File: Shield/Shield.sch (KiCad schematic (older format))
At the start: 0 parts

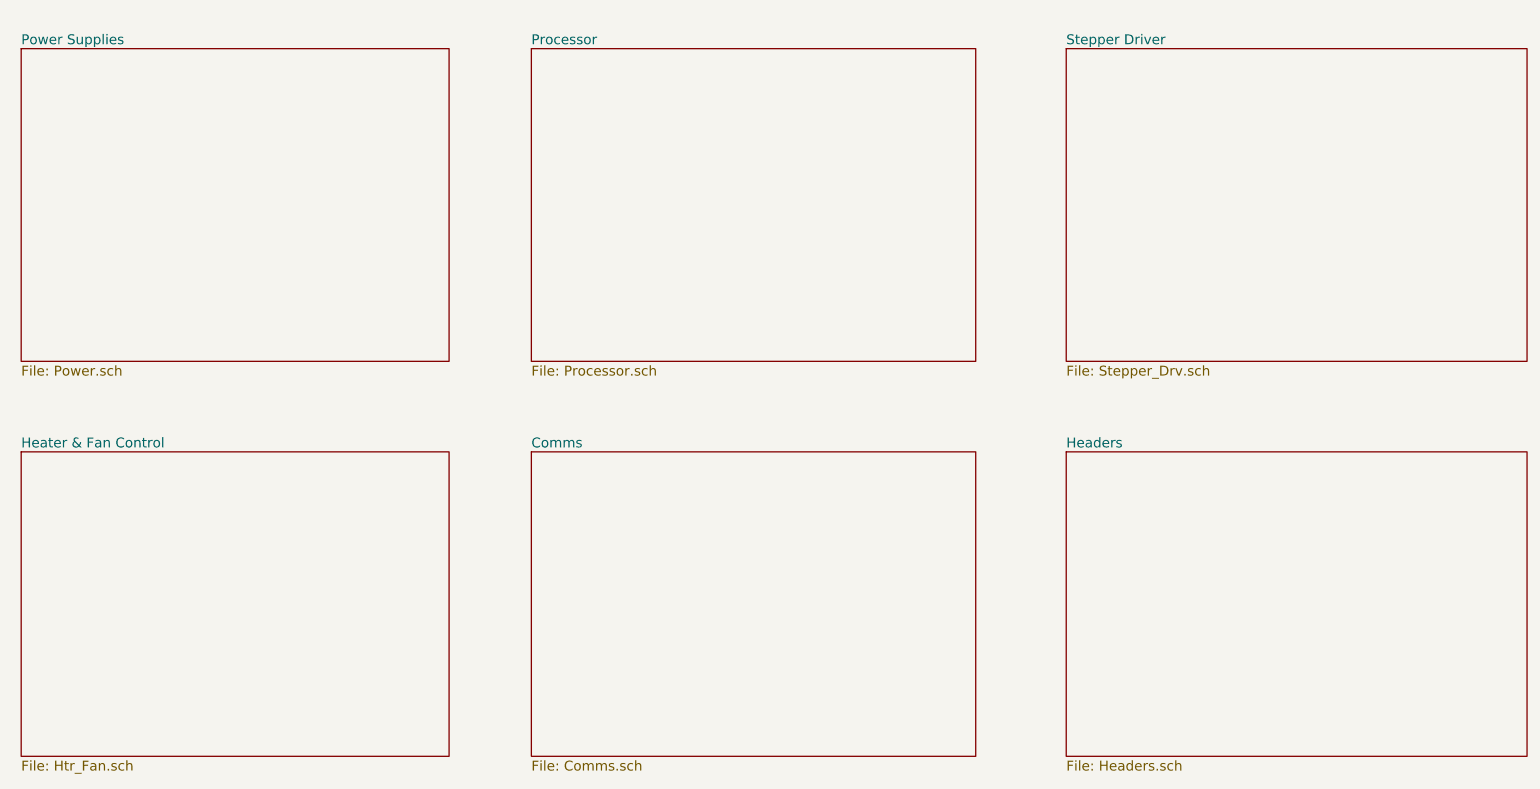
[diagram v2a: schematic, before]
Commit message: First hack at the shield schematic.
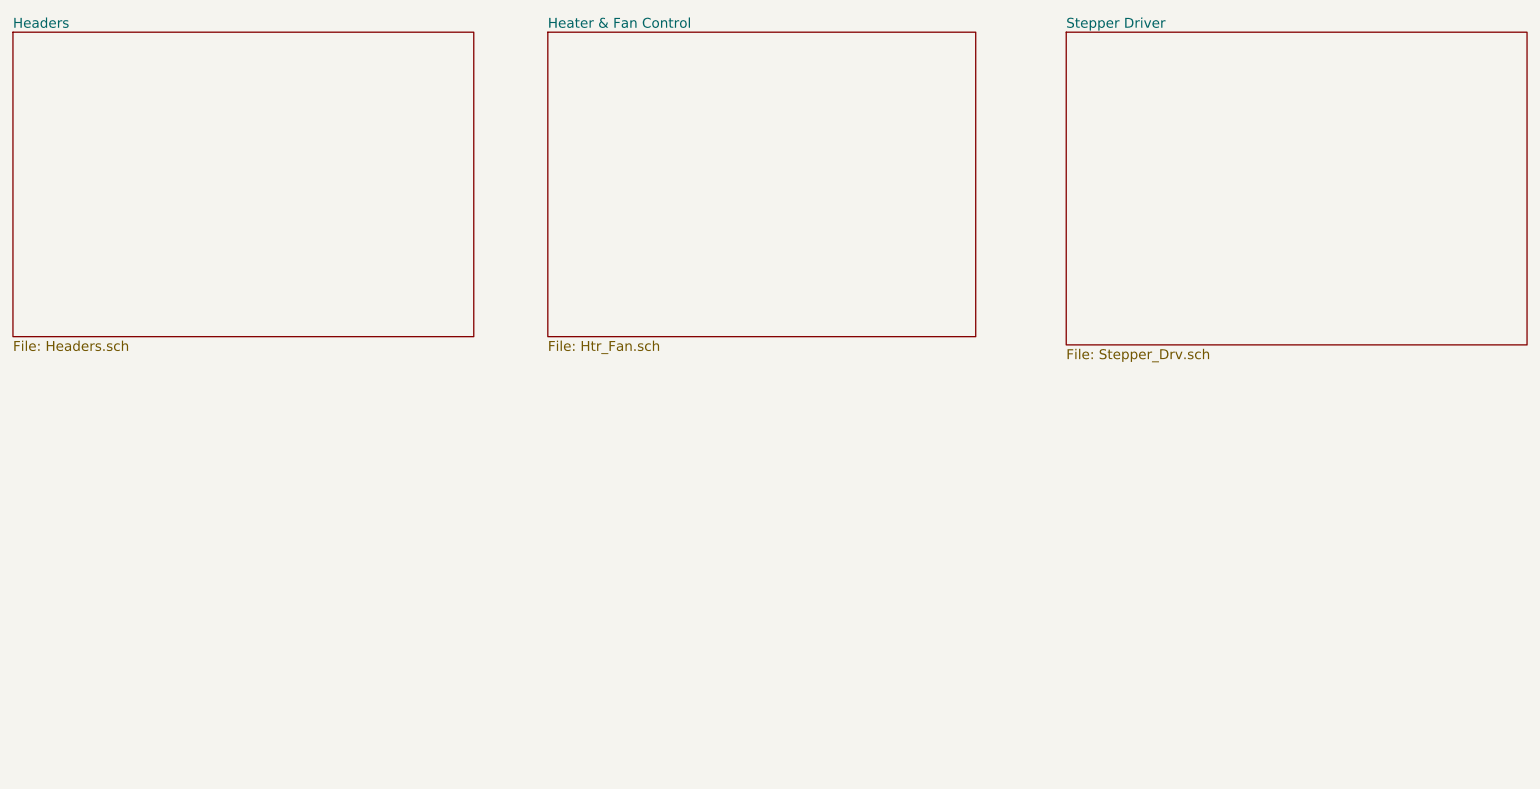
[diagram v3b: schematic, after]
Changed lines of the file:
@@
-EESchema Schematic File Version 2  date Thu 06 Nov 2014 13:12:34 GMT
+EESchema Schematic File Version 2  date Thu 06 Nov 2014 16:31:39 GMT
 LIBS:power
 LIBS:device
@@
 $Descr A4 11700 8267
 encoding utf-8
-Sheet 1 7
+Sheet 1 4
 Title "Duet"
 Date "6 nov 2014"
@@
 $EndDescr
 $Sheet
-S 7850 1250 2800 1900
+S 7850 1150 2800 1900
 U 505779E3
 F0 "Stepper Driver" 60
@@
 $EndSheet
 $Sheet
-S 1500 1250 2600 1900
-U 50522538
-F0 "Power Supplies" 60
-F1 "Power.sch" 60
-$EndSheet
-$Sheet
-S 7850 3700 2800 1850
+S 1450 1150 2800 1850
 U 50656780
 F0 "Headers" 60
@@
 $EndSheet
 $Sheet
-S 4600 3700 2700 1850
-U 50577C6A
-F0 "Comms" 60
-F1 "Comms.sch" 60
-$EndSheet
-$Sheet
-S 1500 3700 2600 1850
+S 4700 1150 2600 1850
 U 50577A22
 F0 "Heater & Fan Control" 60
 F1 "Htr_Fan.sch" 60
 $EndSheet
-$Sheet
-S 4600 1250 2700 1900
-U 50523307
-F0 "Processor" 60
-F1 "Processor.sch" 60
-$EndSheet
 $EndSCHEMATC
